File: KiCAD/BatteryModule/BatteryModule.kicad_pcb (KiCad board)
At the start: 2 copper layers, 90 x 70 mm, 12 parts, among them J1 Power

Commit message: Power Build-1,Battery Build-1完成
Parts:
- added G***: LOGO, LOGO, B.Cu at (137.0, 131.8)
- added G***: LOGO, LOGO, B.Cu at (163.0, 131.2)
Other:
- board text added: "Battery Module Build-1"
- board text added: "SUBARU"
- board text added: "Tokai Student Rocket Project"
- board text added: "V1.3"

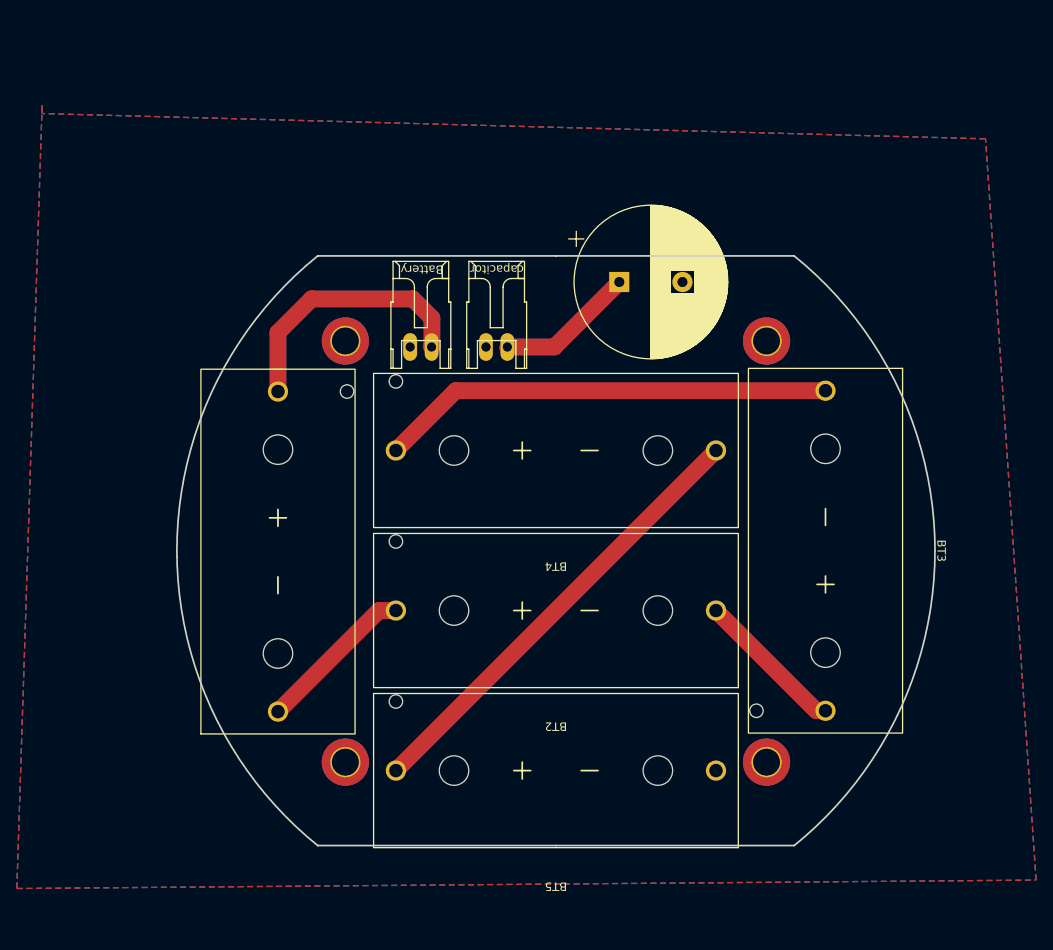
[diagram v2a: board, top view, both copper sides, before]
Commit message: 取付穴位置を変更．キャパシターをSubaru Plateへ移動
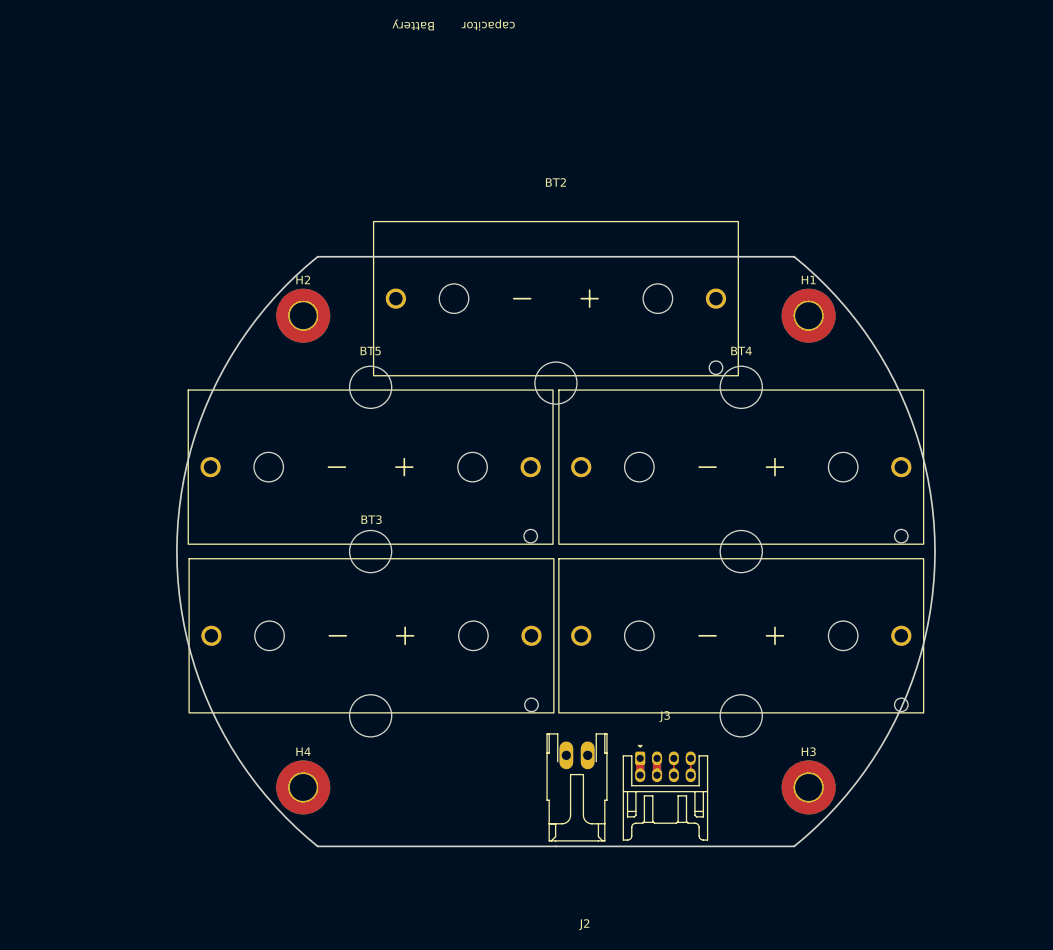
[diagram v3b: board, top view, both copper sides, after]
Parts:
- removed Battery1: Conn_01x02, TSRP_Connector_Hirose:DF1B-2S-2.5R
- removed C1: 2200uF, Capacitor_THT:CP_Radial_D18.0mm_P7.50mm
- removed J1: Power, TSRP_Connector_Hirose:DF1B-2S-2.5R
- removed REF** (x4): MountingHole_3.2mm_M3_DIN965_Pad_TopBottom, MountingHole:MountingHole_3.2mm_M3_DIN965_Pad_TopBottom
- added H1: MountingHole, MountingHole:MountingHole_3.2mm_M3_Pad_TopBottom, F.Cu at (180.0, 72.0)
- added H2: MountingHole, MountingHole:MountingHole_3.2mm_M3_Pad_TopBottom, F.Cu at (120.0, 72.0)
- added H3: MountingHole, MountingHole:MountingHole_3.2mm_M3_Pad_TopBottom, F.Cu at (180.0, 128.0)
- added H4: MountingHole, MountingHole:MountingHole_3.2mm_M3_Pad_TopBottom, F.Cu at (120.0, 128.0)
- added J2: DF1B-2S-2.5R, TSRP_Connector_Hirose:DF1B-2S-2.5R, F.Cu at (152.5, 124.9)
- added J3: DF11-8DP-2DS, TSRP_Connector_Hirose:DF11-8DP-2DS, F.Cu at (163.0, 128.0)
- moved BT1 49.8 mm to (172.0, 119.0), turned to 0 degrees
- moved BT3 48.8 mm to (128.1, 119.0), turned to 0 degrees
- moved BT4 29.7 mm to (172.0, 99.0), turned to 0 degrees
- moved BT5 28.4 mm to (128.0, 99.0), turned to 0 degrees
- moved BT2 19.0 mm to (150.0, 79.0), turned to 0 degrees
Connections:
- BT1 pad 1: Net-(BT1-+) -> /Battery IN
- BT5 pad 2: GND -> /Battery OUT
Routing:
- net Net-(BT3--): track 53.9 -> 0.00 mm
- net Net-(BT4--): track 53.7 -> 0.00 mm
- net Net-(BT1-+): track 31.3 -> 0.00 mm
- net Net-(BT1--): track 19.0 -> 0.00 mm
- net Net-(BT2--): track 17.9 -> 0.00 mm
- net Net-(J1-Pin_1): track 16.5 -> 0.00 mm
- net /GND: track 0.00 -> 2.00 mm
- net /CAN_L: track 0.00 -> 2.00 mm
- net /CAN_H: track 0.00 -> 2.00 mm
- net /12V: track 0.00 -> 2.00 mm
- removed copper zone on B.Cu, net GND
- removed copper zone on F.Cu, net GND
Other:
- outline, holes or cut-outs redrawn

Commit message: 3Dモデルを組み合わせて結合試験する．
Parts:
- removed the G*** at (137.0, 131.8)
- removed the G*** at (163.0, 131.2)
- added D1: Green, LED_SMD:LED_0603_1608Metric_Pad1.05x0.95mm_HandSolder, F.Cu at (169.9, 132.1)
- added G***: LOGO, LOGO, B.Cu at (135.5, 131.3)
- added G***: LOGO, LOGO, B.Cu at (165.0, 131.3)
- added R1: 2.4kR, Resistor_SMD:R_0603_1608Metric_Pad0.98x0.95mm_HandSolder, F.Cu at (171.9, 132.2)
- added TP1: TestPoint, TestPoint:TestPoint_THTPad_D2.0mm_Drill1.0mm, F.Cu at (144.5, 125.7)
- added TP2: TestPoint, TestPoint:TestPoint_THTPad_D2.0mm_Drill1.0mm, F.Cu at (135.9, 125.6)
- moved BT3 45.4 mm to (150.0, 79.3)
- moved BT4 44.0 mm to (128.0, 99.0)
- moved BT2 29.7 mm to (172.0, 99.0)
- moved BT5 20.0 mm to (128.0, 119.0)
- moved BT1 18.0 mm to (172.0, 101.0), turned to 180 degrees
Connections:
- net /GND renamed GND
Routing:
- net /Battery OUT: track 0.00 -> 65.6 mm
- net Net-(BT4--): track 0.00 -> 48.4 mm
- net /Battery IN: track 0.00 -> 27.1 mm
- net Net-(BT3--): track 0.00 -> 26.3 mm
- net Net-(BT2--): track 0.00 -> 26.3 mm
- net Net-(BT1--): track 0.00 -> 22.8 mm
- net /12V: track 2.00 -> 23.1 mm
- net GND: track 2.00 -> 13.8 mm
- net Net-(D1-A): track 0.00 -> 2.78 mm
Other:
- board text added: "12V"
- board text added: "M3"
- board text added: "タイラップ 取付穴"
- board text added: "＋"
- board text added: "－"

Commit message: 3Dモデルを組み合わせて結合試験する
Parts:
- added F1: Polyfuse, Fuse:Fuse_Bourns_MF-RHT300, F.Cu at (134.3, 125.2)
- moved TP2 3.70 mm to (139.6, 125.7)
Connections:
- BT5 pad 2: /Battery OUT -> Net-(BT5--)
- TP2 pad 1: /Battery OUT -> Net-(BT5--)
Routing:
- net /Battery OUT: track 65.6 -> 21.1 mm
- net Net-(BT5--): track 0.00 -> 39.0 mm
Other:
- board text added: "BATTERY"
- board text added: "FUSE"
- board text added: "MAX:30V TRIP:6A"
- board text added: "TEST"
- board text removed: "Battery"
- board text removed: "capacitor"

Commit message: BatteryModule，Build-2完成．今日発注
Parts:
- moved TP1 42.6 mm to (186.9, 121.7)
- moved TP2 26.6 mm to (113.3, 121.7)
- moved J2 21.0 mm to (131.5, 125.2)
- moved F1 8.78 mm to (142.5, 121.9), turned to 0 degrees
- moved BT1 1.03 mm to (172.0, 102.0)
- moved BT5 0.97 mm to (128.0, 120.0)
- moved BT3 0.80 mm to (150.0, 78.5)
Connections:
- BT1 pad 1: /Battery IN -> Net-(BT1-+)
- BT5 pad 2: Net-(BT5--) -> GND
- D1 pad 1: GND -> /BUS_GND
- F1 pad 1: /Battery OUT -> /Battery IN
- F1 pad 2: Net-(BT5--) -> Net-(BT1-+)
- J2 pad 1: /Battery OUT -> GND
- J3 pad 3: GND -> /BUS_GND
- J3 pad 4: GND -> /BUS_GND
- TP2 pad 1: Net-(BT5--) -> GND
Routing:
- net /Battery IN: track 27.1 -> 66.6 mm
- net Net-(BT5--): track 39.0 -> 0.00 mm
- net GND: track 13.8 -> 42.5 mm
- net /Battery OUT: track 21.1 -> 0.00 mm
- net Net-(BT1-+): track 0.00 -> 14.3 mm
- net /BUS_GND: track 0.00 -> 13.8 mm
- net Net-(BT4--): track 48.4 -> 52.9 mm
- net Net-(BT2--): track 26.3 -> 30.6 mm
- net Net-(BT3--): track 26.3 -> 30.6 mm
- net /12V: track 23.1 -> 20.0 mm, vias 0 -> 1
- net Net-(BT1--): track 22.8 -> 23.8 mm
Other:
- outline, holes or cut-outs redrawn
- board text added: "Battery Module Build-2"
- board text added: "リセッタブルヒューズ"
- board text removed: "Battery Module Build-1"
- board text removed: "FUSE"
- board text removed: "MAX:30V TRIP:6A"
